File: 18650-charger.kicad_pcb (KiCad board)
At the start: 4 copper layers, 102.6 x 44.8 mm, 36 parts, among them J1 USB4505-03-0-A_REVA, U1 LTC4121IUDTRPBF, U2 LTC4121IUDTRPBF

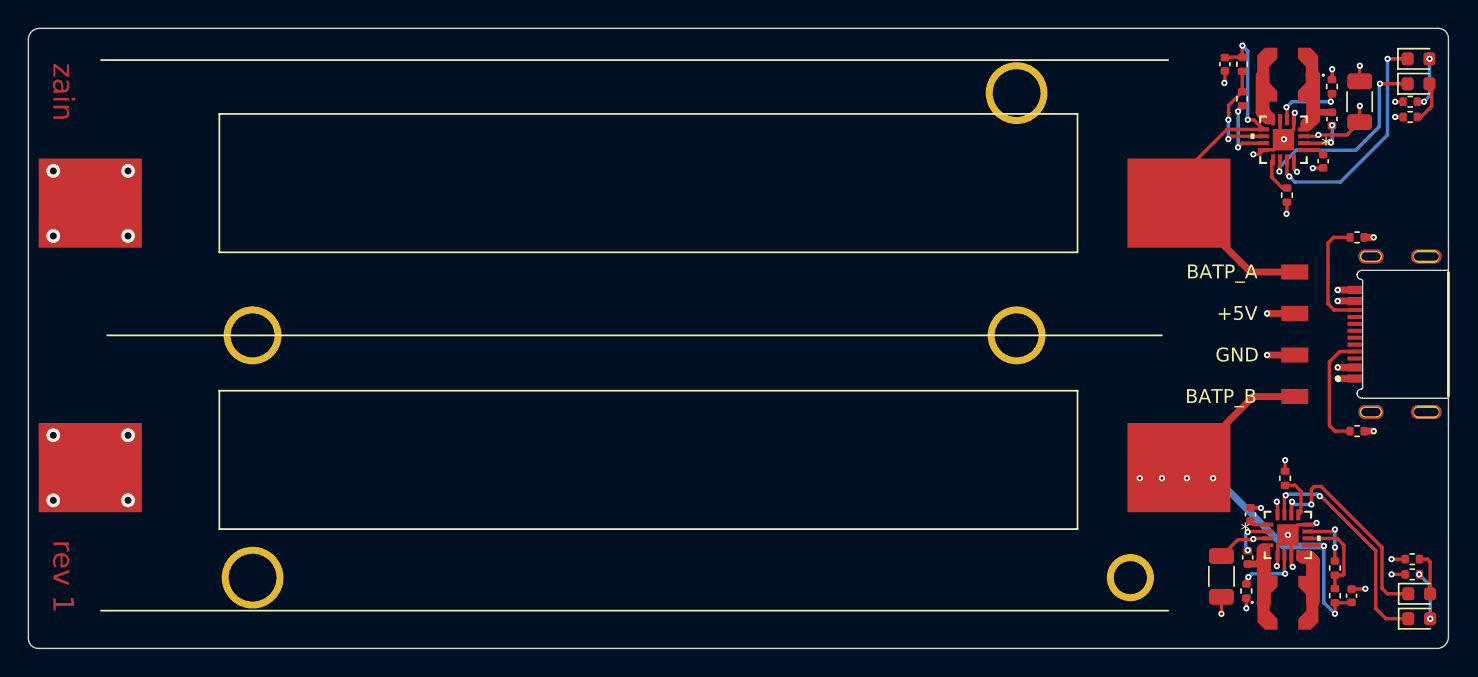
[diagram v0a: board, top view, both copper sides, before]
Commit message: Rev 2, add ideal diode
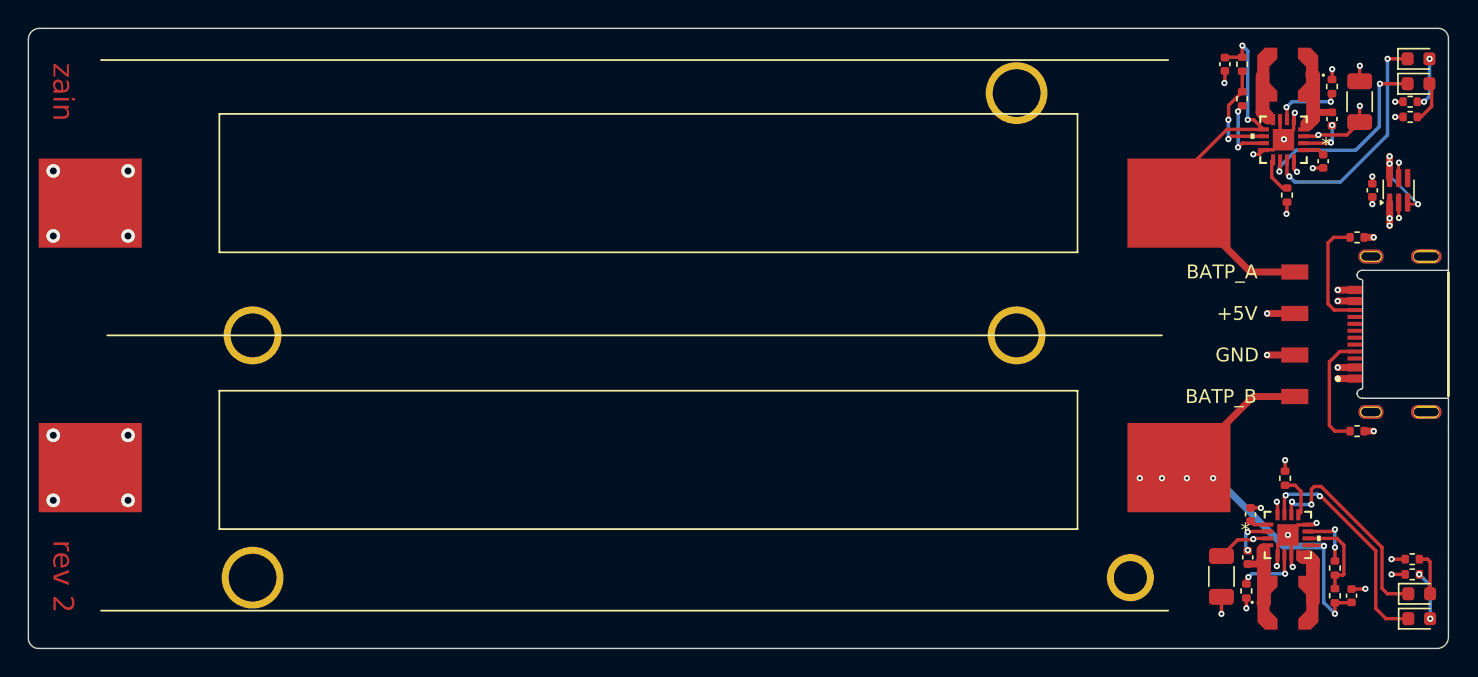
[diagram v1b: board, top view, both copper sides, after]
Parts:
- added C9: 1uF, Capacitor_SMD:C_0402_1005Metric, F.Cu at (206.1, 104.6)
- added U3: LM66100DCK, Package_TO_SOT_SMD:SOT-363_SC-70-6, F.Cu at (208.0, 104.6)
- L3, L6: value 47nH -> 47uH
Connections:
- J1 pad A4_B9: +5V -> /VBUS
- J1 pad B4_A9: +5V -> /VBUS
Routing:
- net /VBUS: track 0.00 -> 4.68 mm, vias 0 -> 5
- net +5V: track 20.5 -> 24.2 mm, vias 14 -> 15
- net GND: track 27.2 -> 30.0 mm, vias 28 -> 31
- added copper zone on In2.Cu, net /VBUS
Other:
- board text added: "rev 2"
- board text removed: "rev 1"
